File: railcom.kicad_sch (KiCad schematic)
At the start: 21 parts, among them U1001 L78L05_TO92, U1002 LM339, U1003 74HC02

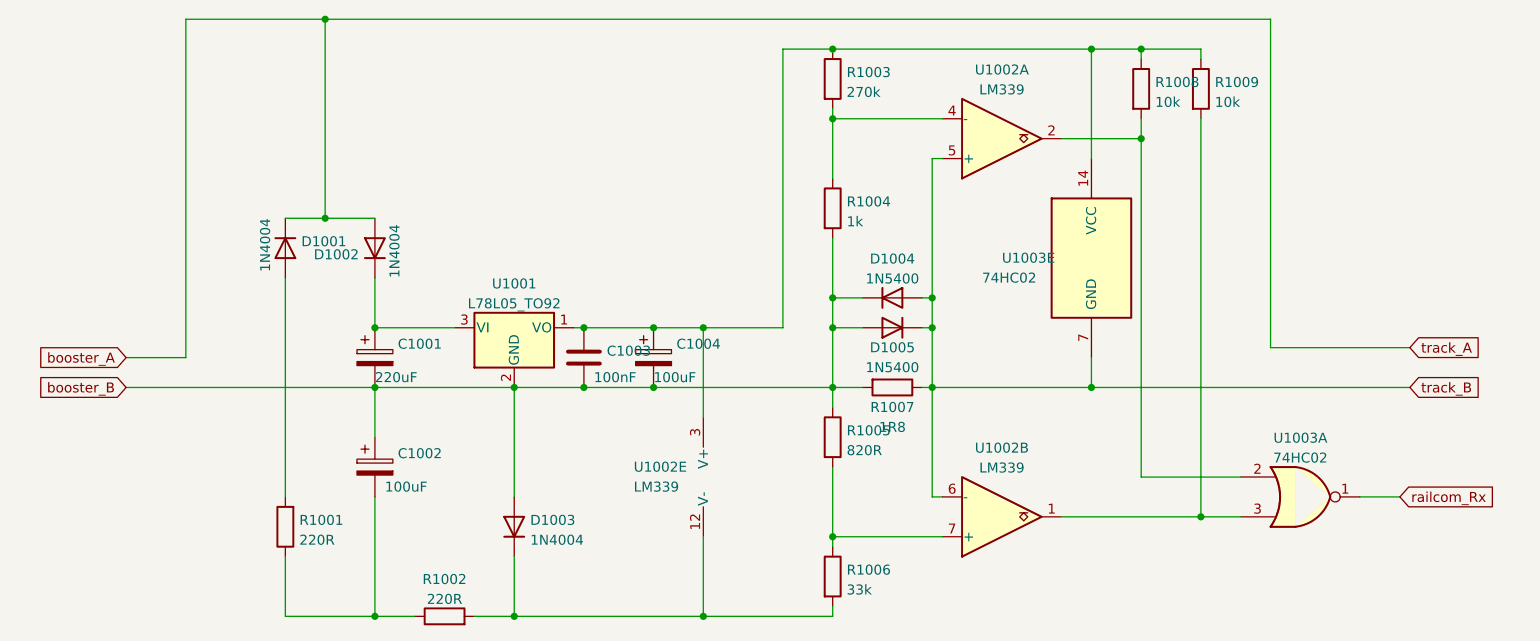
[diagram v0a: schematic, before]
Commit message: added hierarchial labels to some schematics
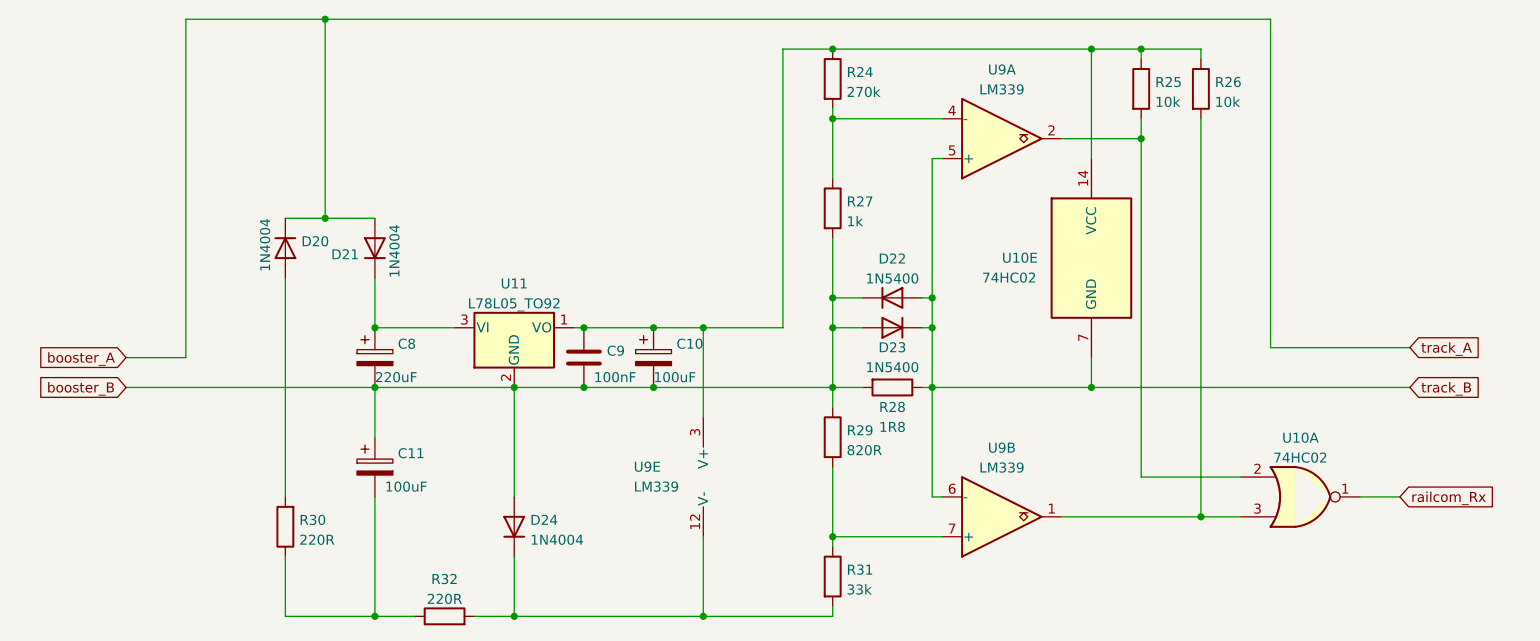
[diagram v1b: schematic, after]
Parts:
- renumbered C1004 to C10, C1002 to C11, C1001 to C8, C1003 to C9, D1001 to D20, D1002 to D21, D1004 to D22, D1005 to D23, D1003 to D24, R1003 to R24, R1008 to R25, R1009 to R26, R1004 to R27, R1007 to R28, R1005 to R29, R1001 to R30, R1006 to R31, R1002 to R32, U1003 to U10, U1001 to U11, U1002 to U9

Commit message: moved some schematic scheets to their own folders and routed a board with it. This allow for re-use of PCB parts.
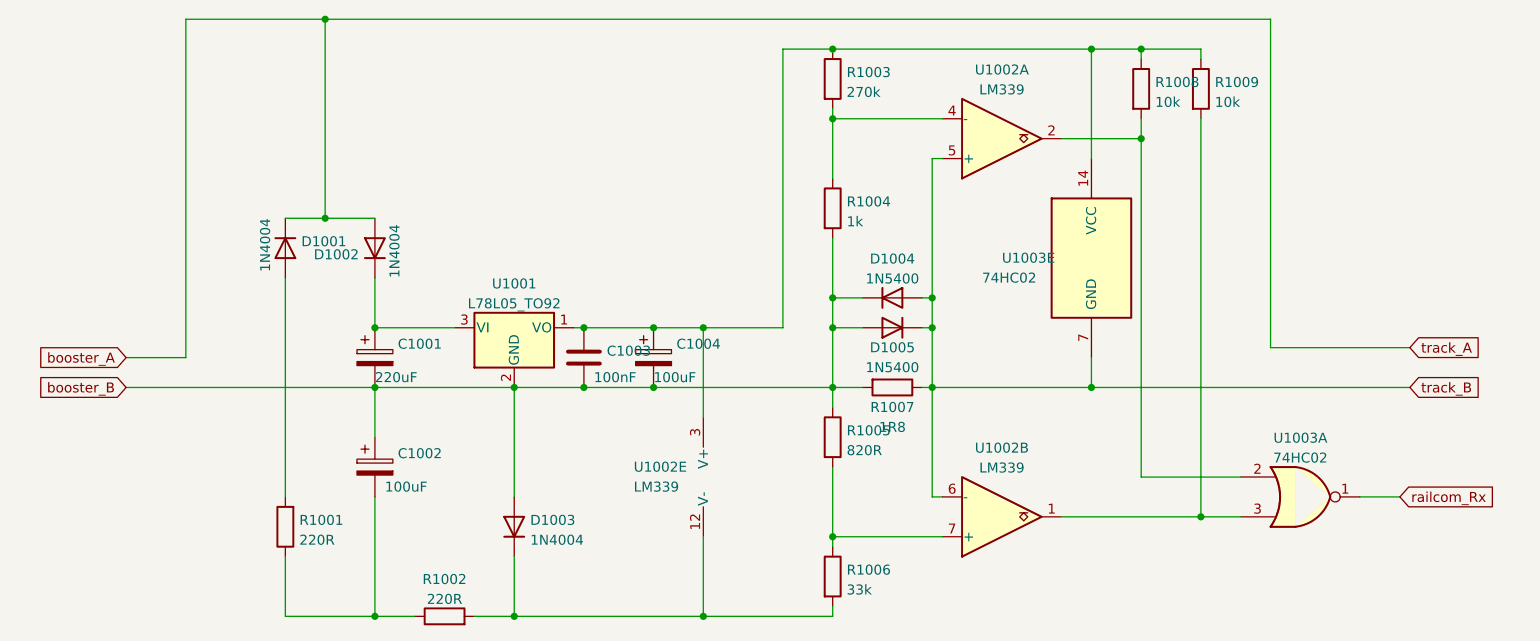
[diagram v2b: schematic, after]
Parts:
- renumbered C8 to C1001, C11 to C1002, C9 to C1003, C10 to C1004, D20 to D1001, D21 to D1002, D24 to D1003, D22 to D1004, D23 to D1005, R30 to R1001, R32 to R1002, R24 to R1003, R27 to R1004, R29 to R1005, R31 to R1006, R28 to R1007, R25 to R1008, R26 to R1009, U11 to U1001, U9 to U1002, U10 to U1003
